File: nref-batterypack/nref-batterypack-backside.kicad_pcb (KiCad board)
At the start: 2 copper layers, 75 x 17 mm, 8 parts, among them J1 C1+, J2 C2-, J3 C3+, J4 C4-, J5 FRONT_CONN

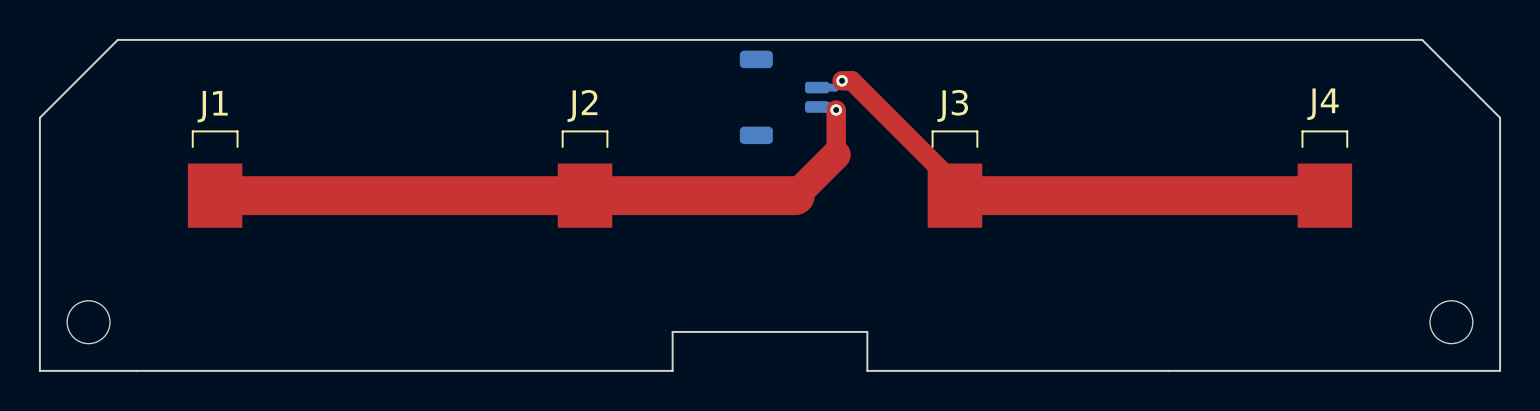
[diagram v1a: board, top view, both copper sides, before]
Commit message: added reverse polarity indicator LEDs
+ silk on the back to indicate cell polarity
+ updated resistor values for balancing
* better b2b chg, dsg fets
+ more testpoints
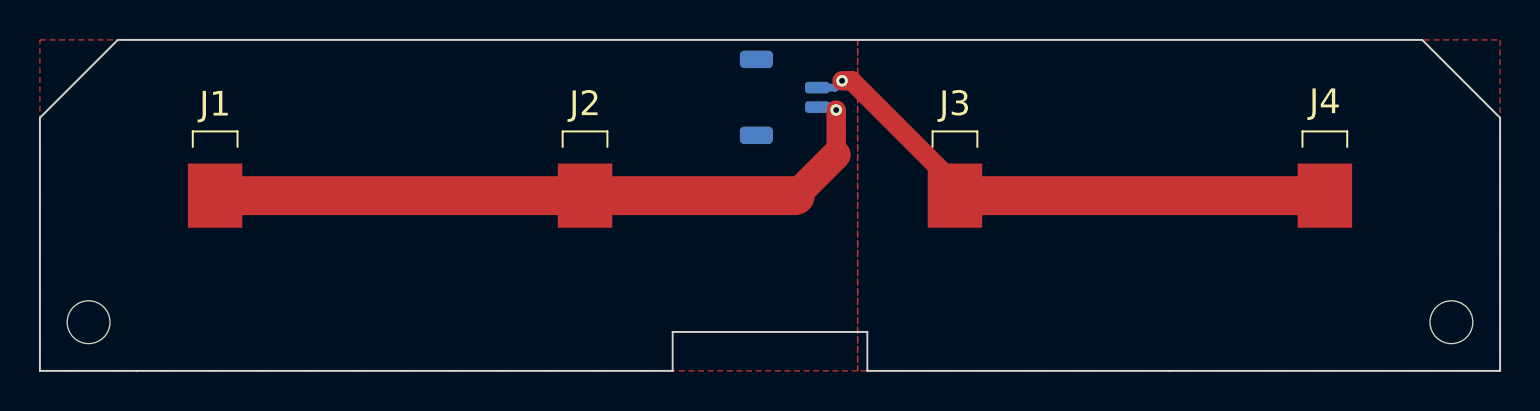
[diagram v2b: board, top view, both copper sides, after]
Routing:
- added copper zone on F.Cu, net /C1+
- added copper zone on F.Cu, net /C3+
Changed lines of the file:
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@@
 		(net 2)
 	)
+	(zone
+		(net 2)
+		(net_name "/C3+")
+		(layer "F.Cu")
+		(hatch edge 0.5)
+		(priority 1)
+		(connect_pads
+			(clearance 0.5)
+		)
+		(min_thickness 0.25)
+		(filled_areas_thickness no)
+		(fill yes
+			(thermal_gap 0.5)
+			(thermal_bridge_width 0.5)
+		)
+		(polygon
+			(pts
+				(xy 132 83) (xy 165 83) (xy 165 100) (xy 132 100)
+			)
+		)
+	)
+	(zone
+		(net 1)
+		(net_name "/C1+")
+		(layer "F.Cu")
+		(hatch edge 0.5)
+		(connect_pads
+			(clearance 0.5)
+		)
+		(min_thickness 0.25)
+		(filled_areas_thickness no)
+		(fill yes
+			(thermal_gap 0.5)
+			(thermal_bridge_width 0.5)
+		)
+		(polygon
+			(pts
+				(xy 90 83) (xy 132 83) (xy 132 100) (xy 90 100)
+			)
+		)
+	)
 )
